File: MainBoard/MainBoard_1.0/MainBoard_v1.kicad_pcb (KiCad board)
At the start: 2 copper layers, 122 x 85.6 mm, 173 parts, among them J1 ILG, J10 SH, J11 SH, J12 SH, J13 FFC, J14 SH, J2 SH, J3 SH, J4 PA, J5 Micro_SD_Card_Det_Hirose_DM3AT, J6 SH, J7 ENC, J8 ENC, J9 PA, Q1 AON7400B, Q10 IRLML6344, Q2 AON7400B, Q3 AON7400B, Q4 AON7400B, Q5 AON7400B, Q6 AON7400B, Q7 2N7002K, Q8 AON7400B, Q9 AON7400B, SW1 SKRPACE010, SW2 SSSS213202, SW3 FR01SC16P-S, SW4 SKRHAAE010, U1 SI7469DP-T1-GE3, U10 DRV8701E, U11 MMC5983MA, U2 LT1963A-TSSOP, U3 TPS62143, U4 ECS-2520S33, U5 INA260, U6 DRV8701E, U7 ICM20648, U8 STM32F469VG, U9 INA260

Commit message: ver_2021
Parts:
- moved R53 3.11 mm to (174.5, 71.1)
- moved Q10 1.80 mm to (174.0, 68.5), turned to 270 degrees
- moved J13 1.50 mm to (165.2, 71.2)
- moved R54 0.22 mm to (174.5, 72.8), turned to 180 degrees
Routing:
- net GND: track 758.3 -> 900.6 mm, vias 43 -> 47
- net +3V3: track 546.8 -> 603.3 mm, vias 29 -> 30
- net +5V: track 265.6 -> 320.6 mm
- net MAKER1: track 65.4 -> 105.7 mm, vias 2 -> 4
- net MAKER2: track 59.9 -> 97.2 mm, vias 1 -> 2
- net AD13: track 92.9 -> 81.1 mm
- net AD4: track 76.0 -> 64.6 mm, vias 2 -> 3
- net AD14: track 94.6 -> 83.9 mm
- net AD11: track 90.7 -> 80.1 mm
- net AD12: track 91.7 -> 81.2 mm
- net SENSOR_PWM: track 77.9 -> 87.9 mm
- net Net-(J13-Pad16): track 0.00 -> 9.80 mm
- net AD9: track 87.6 -> 77.9 mm
- net AD10: track 89.1 -> 79.6 mm
- net AD7: track 87.3 -> 78.8 mm
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- added copper zone on B.Cu, net GND
- added copper zone on F.Cu, net GND

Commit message: update edge
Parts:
- removed REF** (x8): MountingHole_2.2mm_M2, Mounting_Holes:MountingHole_2.2mm_M2
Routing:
- removed copper zone on B.Cu, net GND
- removed copper zone on F.Cu, net GND
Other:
- board size 122 x 85.6 mm -> 120 x 80 mm

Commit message: fixed up_right
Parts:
- moved SW3 57.3 mm to (178.7, 99.3)
- moved J14 18.3 mm to (179.9, 71.2), turned to 270 degrees
- moved J12 17.6 mm to (109.1, 71.2), turned to 90 degrees
- moved C3 12.5 mm to (104.0, 104.3)
- moved C2 12.3 mm to (104.6, 96.9), turned to 90 degrees
- moved R38 6.52 mm to (171.4, 66.7)
- moved R39 6.52 mm to (169.9, 66.7)
- moved R40 4.47 mm to (168.4, 66.7)
- moved R41 4.47 mm to (166.9, 66.7)
- moved R42 4.47 mm to (165.4, 66.7)
- moved R43 4.47 mm to (163.9, 66.7)
- moved R44 3.59 mm to (168.4, 63.8)
- moved R45 3.59 mm to (166.9, 63.8)
- moved R46 3.59 mm to (165.4, 63.8)
- moved R47 3.59 mm to (163.9, 63.8)
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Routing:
- net MAKER1: track 105.7 -> 79.0 mm, vias 4 -> 2
- net AD8: track 79.5 -> 68.1 mm
- net AD7: track 78.8 -> 67.9 mm
- net AD2: track 72.7 -> 62.2 mm
- net AD1: track 72.2 -> 62.9 mm
- net AD10: track 79.6 -> 71.6 mm
- net AD9: track 77.9 -> 70.0 mm
- net +3V3: track 603.3 -> 608.8 mm
- net SENSOR_PWM: track 87.9 -> 83.1 mm
- net AD3: track 66.3 -> 62.2 mm, vias 3 -> 2
- net AD4: track 64.6 -> 61.6 mm, vias 3 -> 2
- net Net-(J13-Pad16): track 9.80 -> 12.6 mm
- net GND: track 900.6 -> 898.4 mm, vias 47 -> 46
- net AD6: track 69.5 -> 68.3 mm
- net AD11: track 80.1 -> 79.0 mm
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
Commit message: fixed right bottom
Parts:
- J3: value SH -> STDC14; footprint Connectors_JST:JST_SH_BM06B-SRSS-TB_06x1.00mm_Straight -> Connector_PinHeader_1.27mm:PinHeader_2x07_P1.27mm_Vertical_SMD
- moved J10 29.6 mm to (161.1, 92.1), turned to 180 degrees
- moved R27 14.4 mm to (161.5, 102.8), turned to 0 degrees
- moved R26 12.9 mm to (161.5, 100.9), turned to 0 degrees
- moved C39 12.3 mm to (158.8, 95.5)
- moved J2 12.0 mm to (181.8, 113.6)
- moved C1 10.8 mm to (181.2, 102.8)
- moved SW1 9.49 mm to (182.1, 99.9), turned to 90 degrees
- moved C38 8.25 mm to (165.9, 95.6)
- moved J8 6.94 mm to (164.5, 97.5)
- moved J7 5.19 mm to (157.3, 97.5)
- moved J3 4.33 mm to (190.2, 110.7)
- moved C33 4.02 mm to (182.9, 134.8), turned to 0 degrees
- moved C12 4.02 mm to (172.5, 107.1), turned to 90 degrees
- moved R24 3.16 mm to (161.5, 99.2)
- moved R25 3.00 mm to (161.5, 97.5)
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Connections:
- J3 pad 1: +3V3 -> Net-(J3-Pad1)
- J3 pad 2: SWCLK -> Net-(J3-Pad2)
- J3 pad 3: GND -> +3V3
- J3 pad 5: NRST -> GND
- J3 pad 6: SWO -> SWCLK
- U7 pad 11: Net-(U7-Pad11) -> GND
- U8 pad 31: R_SW8 -> SW1
- U8 pad 32: R_SW4 -> SW2
- U8 pad 33: R_SW2 -> SW3
- U8 pad 35: R_SW1 -> SW4
- U8 pad 85: SW4 -> R_SW1
- U8 pad 87: SW3 -> R_SW2
- U8 pad 88: SW2 -> R_SW4
- U8 pad 91: SW1 -> R_SW8
- U8 pad 93: ESC2_PWM -> ESC4_PWM
- U8 pad 94: ESC1_PWM -> ESC3_PWM
- U8 pad 98: ESC3_PWM -> ESC2_PWM
- U8 pad 99: ESC4_PWM -> ESC1_PWM
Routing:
- net R_SW8: track 64.4 -> 19.1 mm
- net R_SW4: track 61.6 -> 24.4 mm
- net R_SW2: track 58.9 -> 27.8 mm
- net R_SW1: track 55.8 -> 32.0 mm, vias 0 -> 2
- net ESC4_PWM: track 18.6 -> 41.3 mm
- net ESC3_PWM: track 17.5 -> 38.8 mm
- net ESC2_PWM: track 13.2 -> 33.9 mm
- net +5V: track 321.0 -> 341.3 mm, vias 3 -> 5
- net SW2: track 100.3 -> 82.1 mm
- net ESC1_PWM: track 12.1 -> 30.2 mm
- net SW1: track 95.5 -> 78.7 mm
- net GND: track 898.4 -> 914.5 mm, vias 46 -> 43
- net USART_TX: track 29.2 -> 13.7 mm
- net USART_RX: track 27.6 -> 13.1 mm
- net SW3: track 103.5 -> 90.9 mm
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
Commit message: fixed up right
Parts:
- moved R34 16.0 mm to (157.1, 76.7), turned to 180 degrees
- moved R47 16.0 mm to (173.3, 76.7), turned to 180 degrees
- moved R35 13.9 mm to (157.1, 75.1), turned to 180 degrees
- moved R46 13.8 mm to (173.3, 75.1), turned to 180 degrees
- moved R45 13.4 mm to (170.6, 76.7), turned to 180 degrees
- moved R39 12.4 mm to (162.5, 76.7), turned to 180 degrees
- moved R38 12.2 mm to (162.5, 75.1), turned to 180 degrees
- moved R44 11.5 mm to (170.6, 75.1), turned to 180 degrees
- moved R43 10.8 mm to (167.9, 76.7), turned to 180 degrees
- moved R36 10.2 mm to (159.8, 75.1), turned to 180 degrees
- moved R41 10.1 mm to (165.2, 76.7), turned to 180 degrees
- moved R37 10.0 mm to (159.8, 76.7), turned to 180 degrees
- moved R40 8.99 mm to (165.2, 75.1), turned to 180 degrees
- moved R42 8.76 mm to (167.9, 75.1), turned to 180 degrees
- moved J13 6.54 mm to (164.4, 67.1)
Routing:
- net GND: track 914.5 -> 899.0 mm, vias 43 -> 44
- net AD14: track 83.4 -> 96.3 mm
- net AD12: track 80.4 -> 92.7 mm
- net AD13: track 81.5 -> 91.7 mm
- net +5V: track 341.3 -> 332.4 mm
- net AD1: track 68.0 -> 59.5 mm
- net MAKER2: track 97.2 -> 88.9 mm
- net AD10: track 71.6 -> 79.5 mm
- net AD2: track 67.3 -> 59.5 mm
- net AD8: track 71.7 -> 77.0 mm
- net AD5: track 72.2 -> 67.7 mm
- net AD4: track 66.8 -> 71.2 mm
- net SENSOR_PWM: track 83.1 -> 86.2 mm
- net AD3: track 67.4 -> 64.5 mm
- net Net-(J13-Pad16): track 12.6 -> 15.3 mm, vias 0 -> 2
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
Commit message: wiring completed
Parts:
- moved C2 30.6 mm to (119.4, 123.7), turned to 270 degrees
- moved C3 21.5 mm to (113.8, 123.4), turned to 270 degrees
- moved C51 11.5 mm to (119.1, 74.4), turned to 180 degrees
- moved C49 9.55 mm to (119.1, 72.6), turned to 180 degrees
- moved SW4 8.94 mm to (126.4, 71.4), turned to 45 degrees
- moved C48 6.48 mm to (119.1, 70.9), turned to 180 degrees
- moved C50 3.81 mm to (119.1, 69.2), turned to 0 degrees
- moved C47 3.55 mm to (119.1, 67.5), turned to 0 degrees
- moved J4 1.60 mm to (132.1, 91.7)
- moved J9 1.60 mm to (125.6, 91.7)
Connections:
- U8 pad 31: SW1 -> SW4
- U8 pad 32: SW2 -> SW5
- U8 pad 35: SW4 -> SW1
- U8 pad 84: SW5 -> SW2
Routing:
- net GND: track 899.0 -> 947.9 mm, vias 44 -> 51
- net +3V3: track 600.5 -> 561.0 mm
- net +5V: track 332.4 -> 356.5 mm
- net SW3: track 90.9 -> 67.4 mm
- net SW5: track 90.7 -> 69.3 mm
- net SW1: track 78.7 -> 69.5 mm
- net SW4: track 76.1 -> 70.0 mm
- net MAKER1: track 82.4 -> 80.0 mm
- net AD1: track 59.5 -> 57.3 mm
- net MAKER2: track 88.9 -> 86.7 mm
- net AD2: track 59.5 -> 57.5 mm
- net AD10: track 79.5 -> 77.5 mm
- net AD5: track 67.7 -> 65.7 mm
- net AD9: track 74.0 -> 72.0 mm
- net AD4: track 71.2 -> 69.2 mm
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- added copper zone on B.Cu, net GND
- added copper zone on F.Cu, net GND

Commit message: fixed main_board
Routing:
- net +3V3: track 561.0 -> 546.1 mm
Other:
- outline, holes or cut-outs redrawn

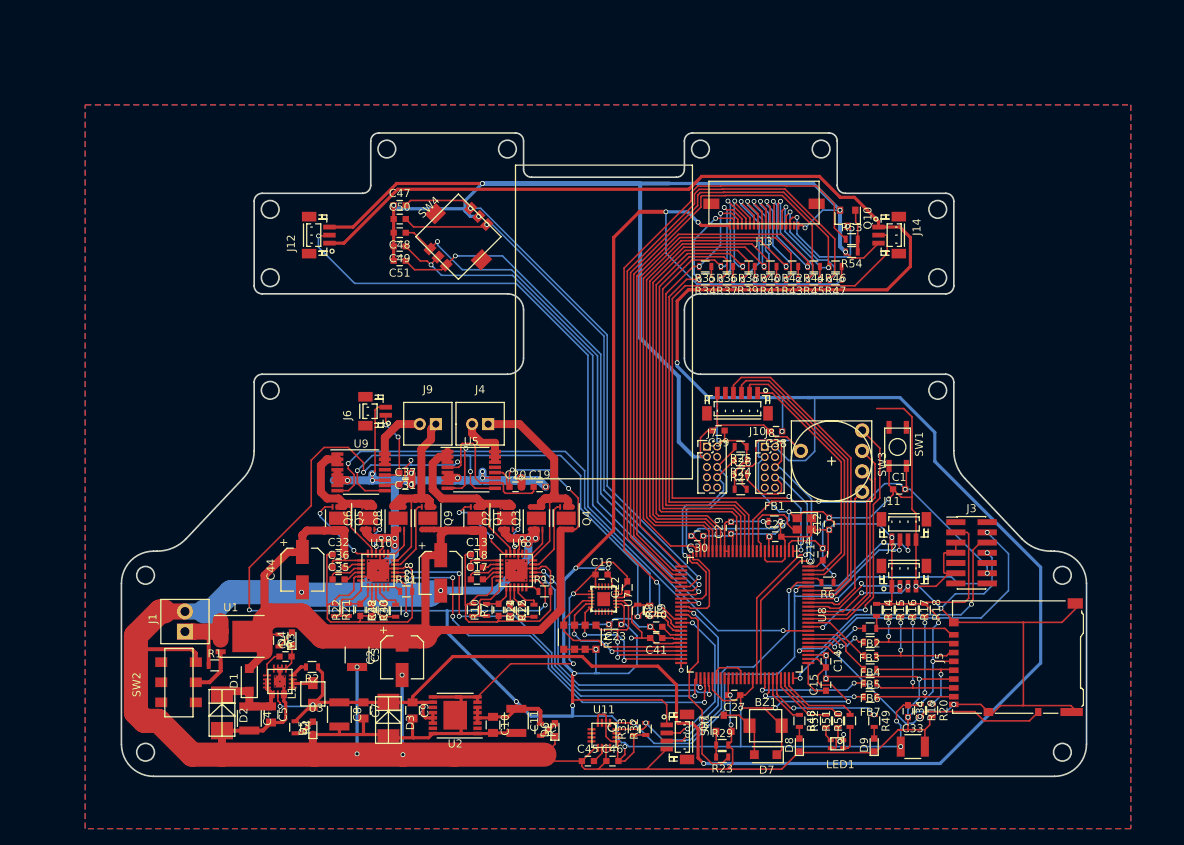
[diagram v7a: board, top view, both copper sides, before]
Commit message: remove antena and move referencse by main board
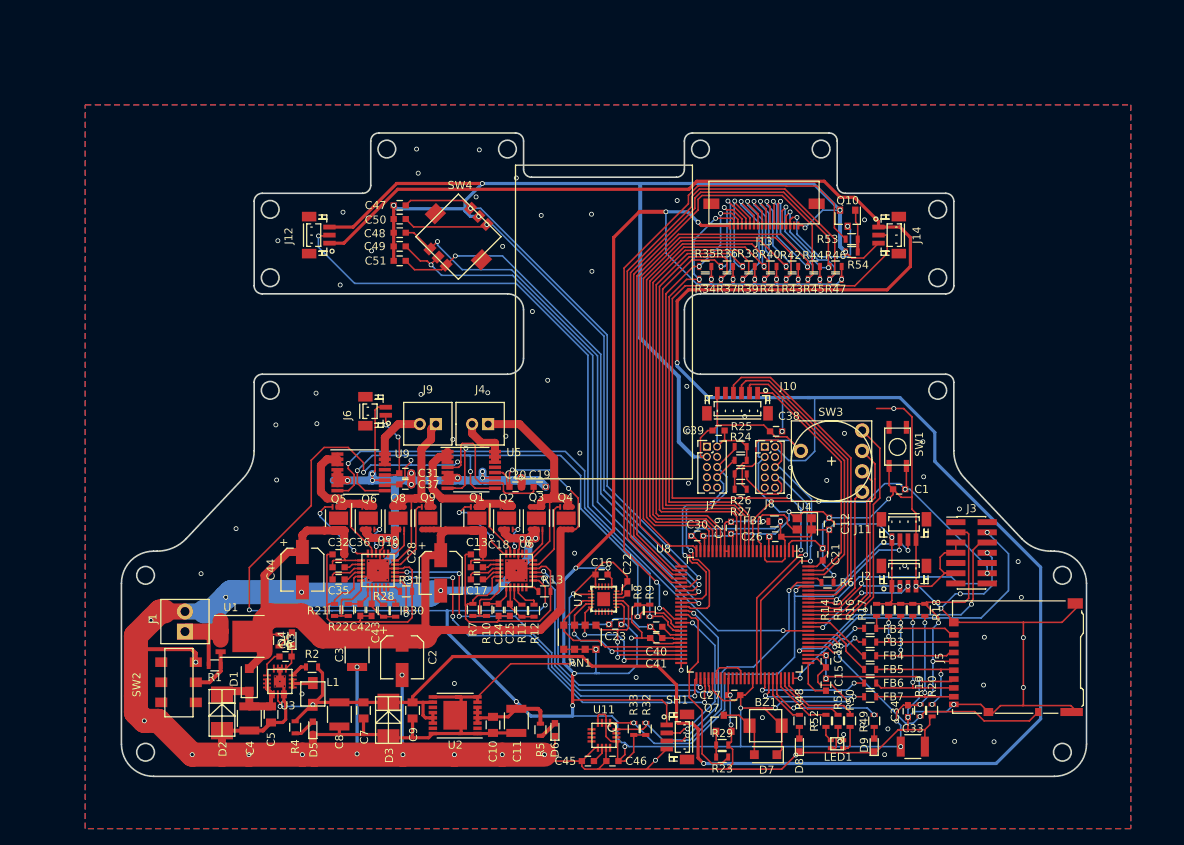
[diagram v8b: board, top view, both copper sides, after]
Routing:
- net GND: track 947.9 -> 930.7 mm, vias 51 -> 122
- net +5V: track 356.5 -> 360.0 mm
